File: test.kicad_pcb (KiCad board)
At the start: 2 copper layers, 45.7 x 27.9 mm, 32 parts, among them J1 ICSP, J2 SPI, J3 UART, J4 3.3v VDD, J5 VSS, J6 GPIO Header, J7 I2C, SW1 Reset Button, U1 PIC32MX340F512H-80I_MR

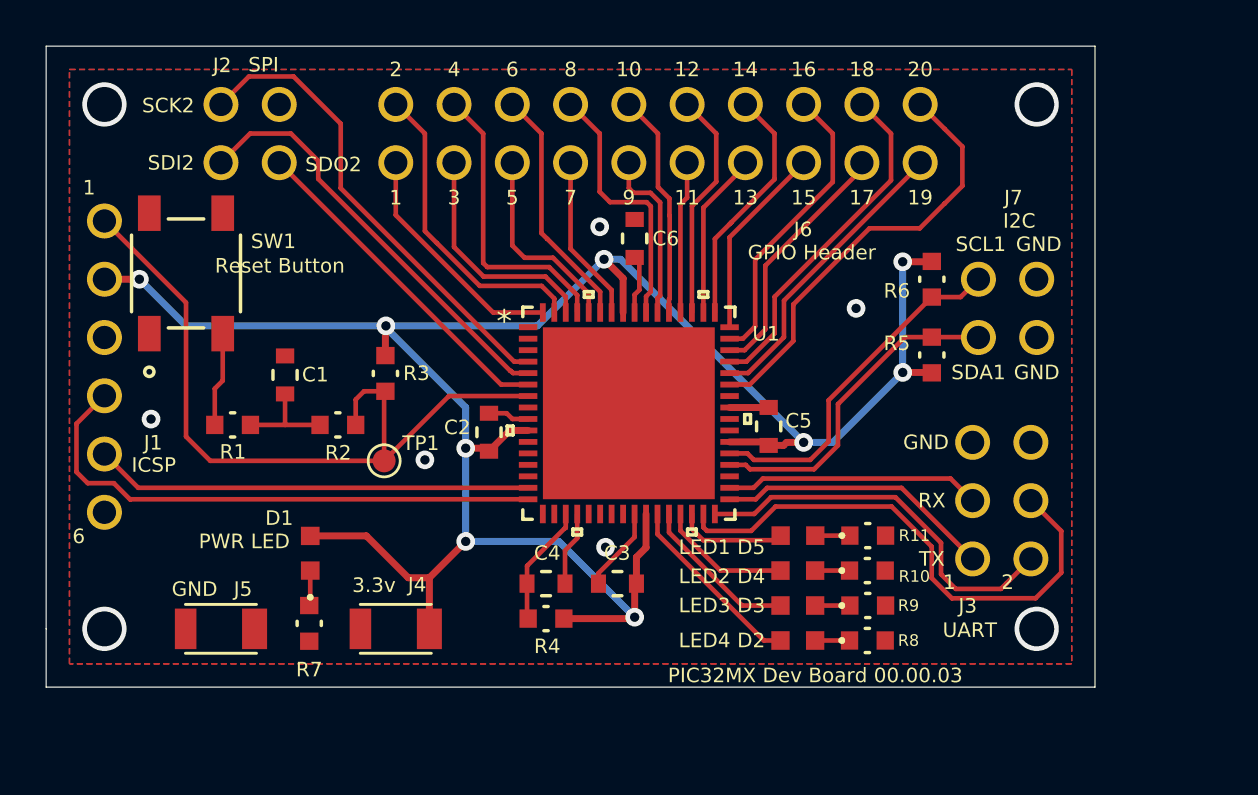
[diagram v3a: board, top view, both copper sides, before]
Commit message: - Changed PIC from MR to PT package for ease of soldering - Increased size from 2"-1.2"
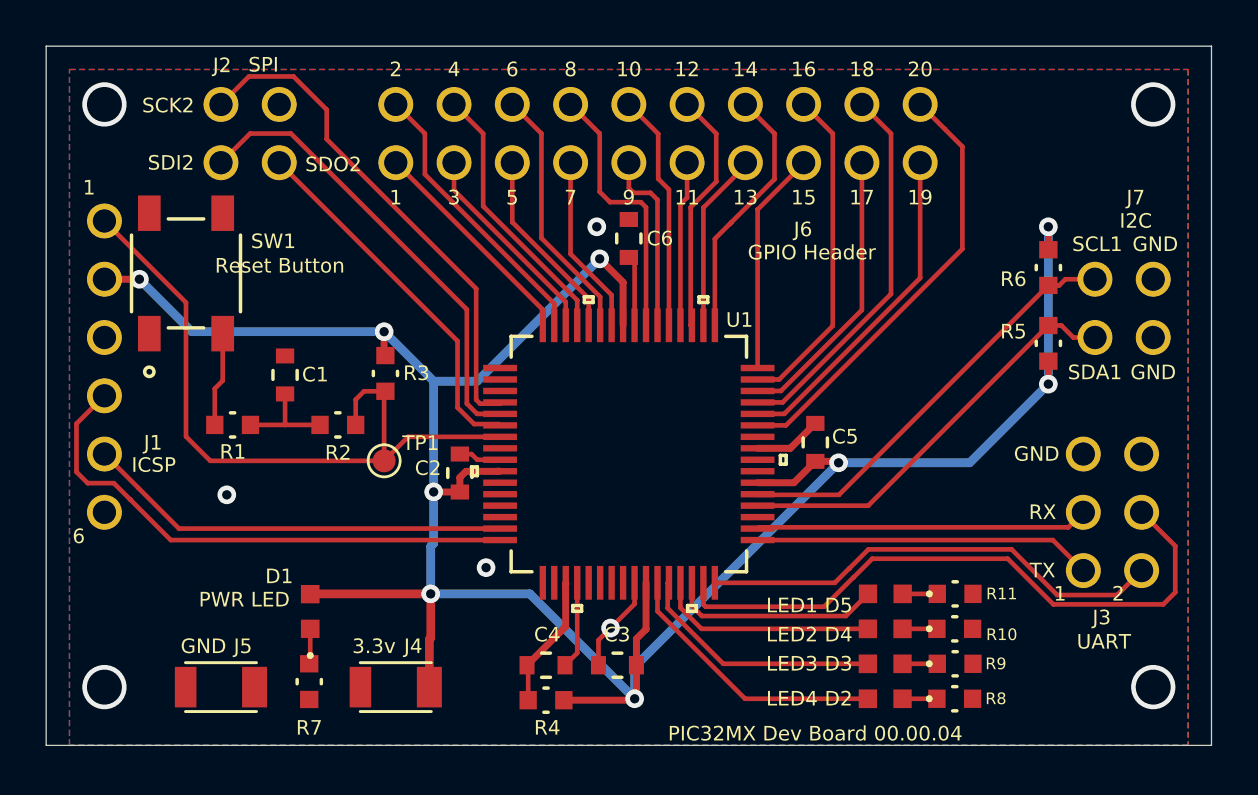
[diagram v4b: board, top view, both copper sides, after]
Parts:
- U1: value PIC32MX340F512H-80I_MR -> PIC32MX340F512H-80V_PT; footprint mod:PIC32MX340F512H-80I&slash_MR -> mod:PIC32MX340F512H-80V&slash_PT
- moved R5 5.11 mm to (180.8, 104.4)
- moved R6 5.11 mm to (180.8, 101.1)
- moved J7 5.08 mm to (182.9, 101.6)
- moved J3 4.85 mm to (182.4, 114.3)
- moved D2 4.58 mm to (173.7, 119.9)
- moved D3 4.58 mm to (173.7, 118.4)
- moved D4 4.58 mm to (173.7, 116.8)
- moved R10 4.58 mm to (176.8, 116.8)
- moved R11 4.58 mm to (176.8, 115.3)
- moved R8 4.58 mm to (176.8, 119.9)
- moved R9 4.58 mm to (176.8, 118.4)
- moved D5 4.58 mm to (173.7, 115.3)
- moved C3 3.56 mm to (162.1, 118.4)
- moved C4 3.56 mm to (158.9, 118.4)
- moved R4 3.56 mm to (158.9, 120.0)
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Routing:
- net +3V3: track 97.3 -> 109.1 mm
- net Net-(D5-Pad2): track 4.81 -> 9.27 mm
- net Net-(J3-Pad3): track 23.3 -> 27.6 mm
- net Net-(D3-Pad2): track 6.98 -> 10.9 mm
- net Net-(D4-Pad2): track 5.81 -> 9.64 mm
- net Net-(D2-Pad2): track 8.16 -> 12.0 mm
- net Net-(J7-Pad1): track 14.4 -> 18.2 mm
- net Net-(J3-Pad1): track 17.1 -> 20.5 mm
- net Net-(J3-Pad4): track 11.2 -> 14.5 mm
- net Net-(J7-Pad2): track 15.3 -> 18.6 mm
- net Net-(J3-Pad2): track 12.1 -> 14.7 mm
- net GNDREF: track 10.5 -> 12.9 mm, vias 9 -> 8
- net Net-(J1-Pad1): track 33.0 -> 31.0 mm
- net Net-(J6-Pad17): track 10.9 -> 12.7 mm
- net Net-(J6-Pad19): track 13.1 -> 14.6 mm
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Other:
- board size 45.7 x 27.9 mm -> 50.8 x 30.5 mm
- board text added: "PIC32MX Dev Board 00.00.04"
- board text removed: "PIC32MX Dev Board 00.00.03"

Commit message: Made a few changes for boardhouse - Moved title silkscreen up like 10mil - Shifted mount holes from vias to an actual footprint
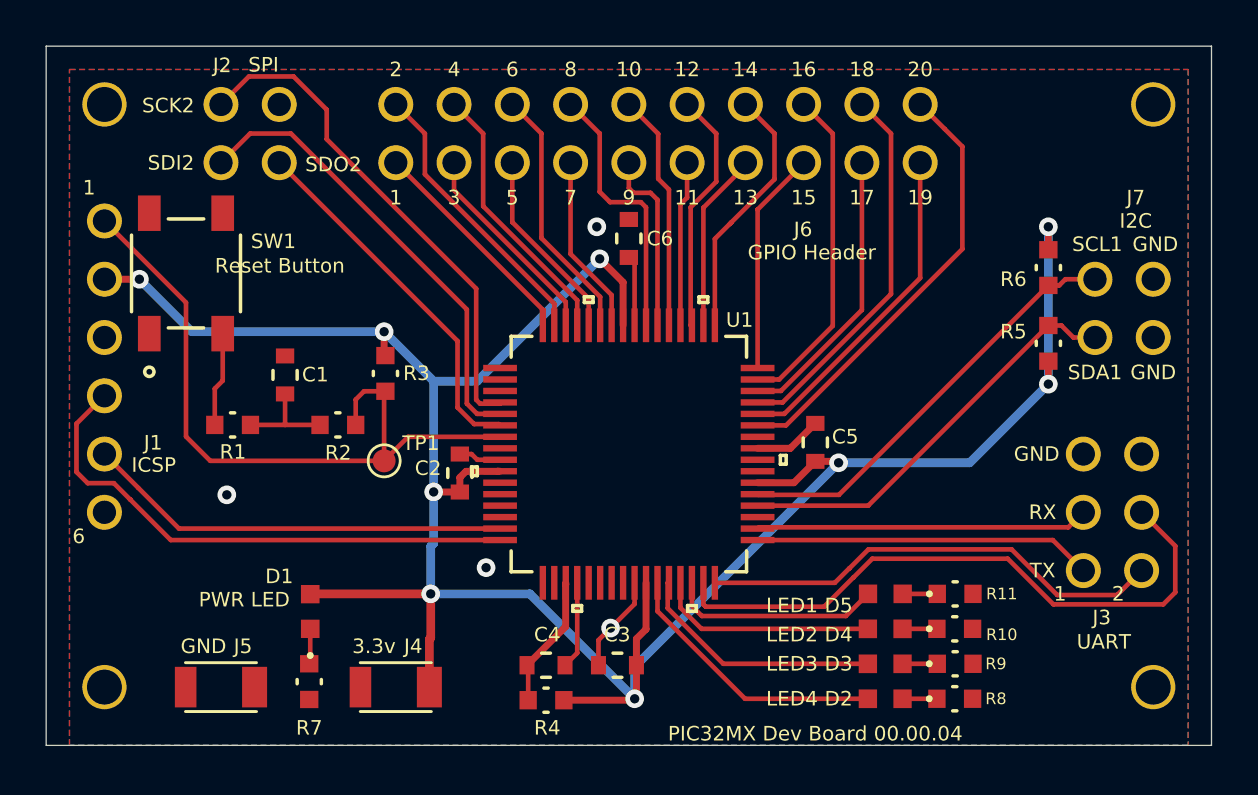
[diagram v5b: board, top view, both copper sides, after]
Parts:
- added H1: MountingHole_Pad, mod:test, F.Cu at (139.7, 94.0)
- added H2: MountingHole_Pad, mod:test, F.Cu at (185.4, 119.4)
- added H3: MountingHole_Pad, mod:test, F.Cu at (185.4, 94.0)
- added H4: MountingHole_Pad, mod:test, F.Cu at (139.7, 119.4)
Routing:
- net GNDREF: vias 8 -> 4
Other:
- rule pad_to_mask_clearance: 0.2 -> 0

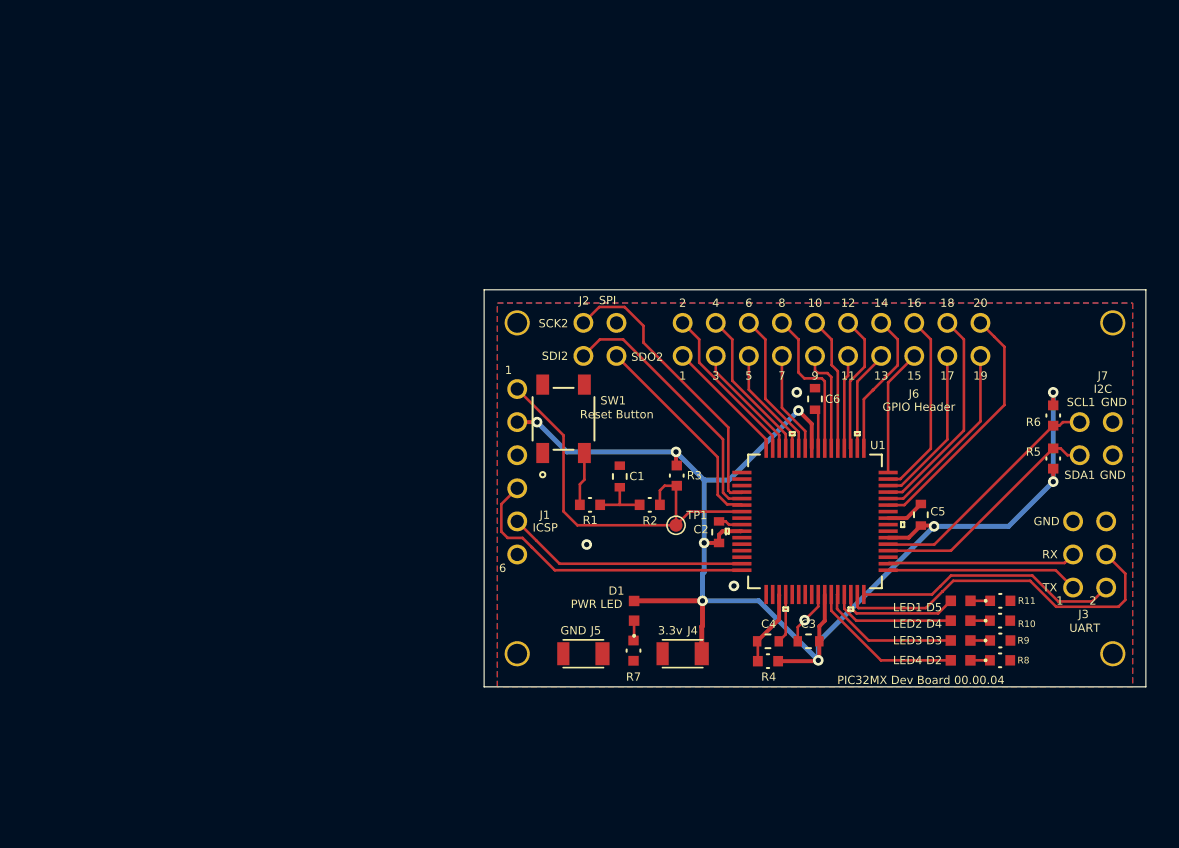
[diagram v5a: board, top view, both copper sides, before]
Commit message: - Began work on dev board V2
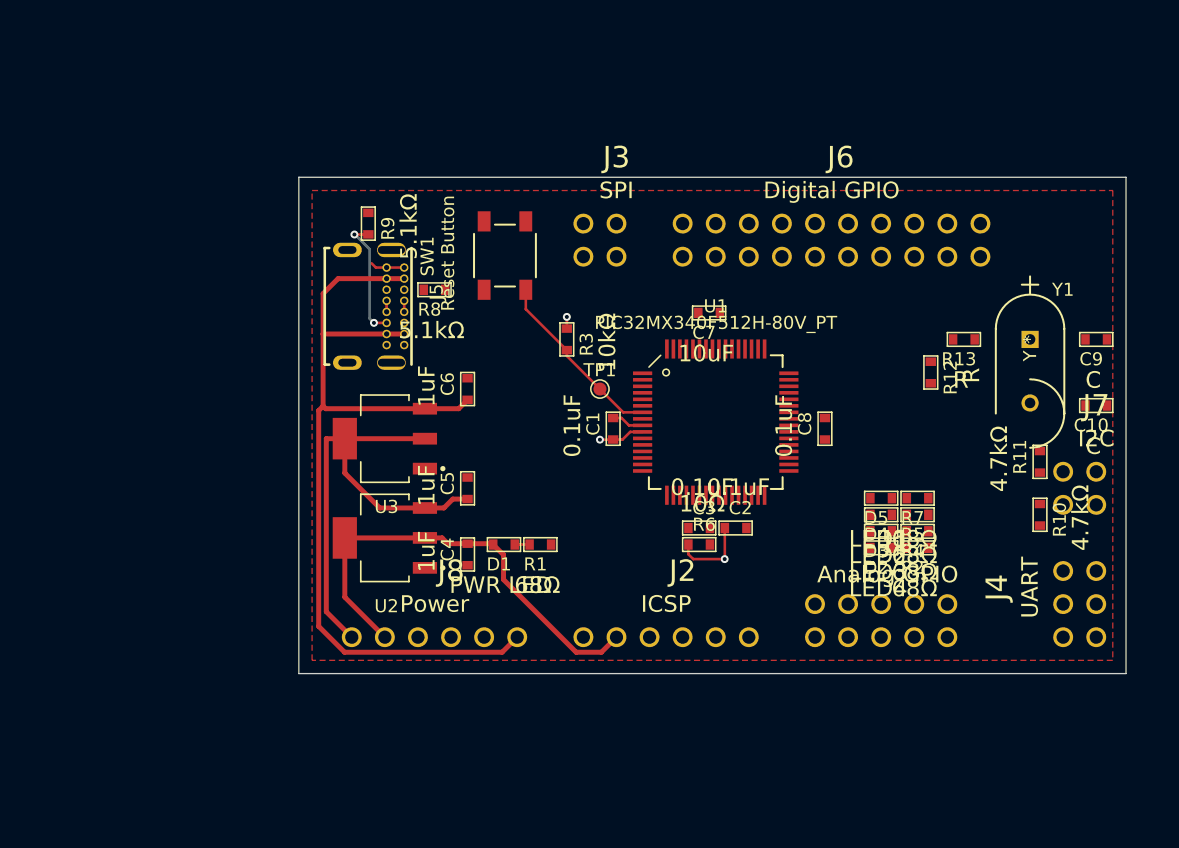
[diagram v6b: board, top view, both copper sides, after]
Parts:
- removed H1, H2, H3, H4: MountingHole_Pad, mod:test
- added C10: C, mod:0603, F.Cu at (184.2, 100.3)
- added C7: 10uF, mod:0603, F.Cu at (154.4, 93.2)
- added C8: 0.1uF, mod:0603, F.Cu at (163.3, 102.1)
- added C9: C, mod:0603, F.Cu at (184.2, 95.2)
- added J8: Power, mod:01x06, F.Cu at (127.0, 118.1)
- added R12: R, mod:0603, F.Cu at (171.4, 97.8)
- added R13: R, mod:0603, F.Cu at (174.0, 95.2)
- added U2: AZ1117EH-3.3TRG1, mod:SOT230P700X180-4N, F.Cu at (129.5, 110.5)
- added U3: AZ1117EH-5.0TRG1, mod:SOT230P700X180-4N, F.Cu at (129.5, 102.9)
- added Y1: Y, mod:9B-8.000MAAJ-B, F.Cu at (179.1, 95.2)
- C1, C2, C3: footprint mod:CL10A106MQ8NNNC -> mod:0603
- C4, C5: value 0.1uF -> 1uF; footprint mod:CL10A106MQ8NNNC -> mod:0603
- C6: value 10uF -> 1uF; footprint mod:CL10A106MQ8NNNC -> mod:0603
- D1, D2, D3, D4, D5: footprint mod:LTST-C191KGKT -> mod:0603
- J1: value ICSP -> Analog GPIO; footprint mod:01x06 -> mod:02x05
- J2: value SPI -> ICSP; footprint mod:02x02 -> mod:01x06
- J3: value UART -> SPI; footprint mod:02x03 -> mod:02x02
- J4: value 3.3v VDD -> UART; footprint mod:RESC3115X65N -> mod:02x03
- J5: value VSS -> USB4085-GF-A_REVA; footprint mod:RESC3115X65N -> mod:GCT_USB4085-GF-A_REVA
- J6: value GPIO Header -> Digital GPIO
- R1, R2: value 470Ω -> 68Ω; footprint mod:ERJ-3EKF10R0V -> mod:0603
- R10, R11: value 68Ω -> 4.7kΩ; footprint mod:ERJ-3EKF10R0V -> mod:0603
- R3, R7: footprint mod:ERJ-3EKF10R0V -> mod:0603
- R4: value 10Ω -> 68Ω; footprint mod:ERJ-3EKF10R0V -> mod:0603
- R5: value 4.7kΩ -> 68Ω; footprint mod:ERJ-3EKF10R0V -> mod:0603
- R6: value 4.7kΩ -> 10Ω; footprint mod:ERJ-3EKF10R0V -> mod:0603
- R8, R9: value 68Ω -> 5.1kΩ; footprint mod:ERJ-3EKF10R0V -> mod:0603
- moved R9 58.1 mm to (128.3, 86.4), turned to 270 degrees
- moved R8 51.9 mm to (133.3, 91.4)
- moved J3 46.8 mm to (144.8, 86.4), turned to 0 degrees
- moved C5 34.9 mm to (135.9, 106.7)
- moved J5 32.1 mm to (127.0, 92.7), turned to 270 degrees
- moved J4 29.2 mm to (181.6, 118.1), turned to 90 degrees
- moved R6 28.9 mm to (153.7, 111.0), turned to 0 degrees
- moved J1 28.2 mm to (162.6, 115.6), turned to 0 degrees
- moved C6 26.7 mm to (135.9, 99.1)
- moved R7 24.7 mm to (170.4, 107.4), turned to 180 degrees
- moved J2 24.1 mm to (144.8, 118.1)
- moved C4 24.0 mm to (135.9, 111.8), turned to 90 degrees
- moved R2 20.8 mm to (170.4, 111.3), turned to 180 degrees
- moved R4 15.2 mm to (170.4, 110.0)
- moved R3 13.4 mm to (143.5, 95.2)
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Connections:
- C1 pad 1: GNDREF -> +3V3
- C1 pad 2: Net-(C1-Pad2) -> GNDREF
- C3 pad 1: +3V3 -> GNDREF
- C3 pad 2: GNDREF -> Net-(C3-Pad2)
- C4 pad 2: Net-(C4-Pad2) -> +3V3
- C5 pad 1: +3V3 -> +5V
- C6 pad 1: Net-(C6-Pad1) -> VCC
- J1 pad 2: +3V3 -> Net-(J1-Pad2)
- J1 pad 3: GNDREF -> Net-(J1-Pad3)
- J2 pad 2: Net-(J2-Pad2) -> +3V3
- J2 pad 3: Net-(J2-Pad3) -> GNDREF
- J4 pad 1: +3V3 -> Net-(J4-Pad1)
- R1 pad 1: Net-(R1-Pad1) -> GNDREF
- R1 pad 2: Net-(C1-Pad2) -> Net-(D1-Pad1)
- R10 pad 1: GNDREF -> Net-(J7-Pad1)
- R10 pad 2: Net-(D4-Pad1) -> +3V3
- R11 pad 1: GNDREF -> Net-(J7-Pad2)
- R11 pad 2: Net-(D5-Pad1) -> +3V3
- R2 pad 1: Net-(C1-Pad2) -> GNDREF
- R2 pad 2: Net-(J1-Pad1) -> Net-(D2-Pad1)
- R3 pad 2: Net-(J1-Pad1) -> Net-(J2-Pad1)
- R4 pad 1: +3V3 -> GNDREF
- R4 pad 2: Net-(C4-Pad2) -> Net-(D3-Pad1)
- R5 pad 1: Net-(J7-Pad1) -> GNDREF
- R5 pad 2: +3V3 -> Net-(D4-Pad1)
- R6 pad 1: Net-(J7-Pad2) -> +3V3
- R6 pad 2: +3V3 -> Net-(C3-Pad2)
- R7 pad 2: Net-(D1-Pad1) -> Net-(D5-Pad1)
- R8 pad 2: Net-(D2-Pad1) -> Net-(J5-PadA5)
- R9 pad 2: Net-(D3-Pad1) -> Net-(J5-PadB5)
- SW1 pad 3: Net-(R1-Pad1) -> Net-(J2-Pad1)
- TP1 pad 1: Net-(J1-Pad1) -> Net-(J2-Pad1)
- U1 pad 11: Net-(U1-Pad11) -> Net-(J1-Pad6)
- U1 pad 12: Net-(U1-Pad12) -> Net-(J1-Pad5)
- U1 pad 13: Net-(U1-Pad13) -> Net-(J1-Pad4)
- U1 pad 14: Net-(U1-Pad14) -> Net-(J1-Pad3)
- U1 pad 15: Net-(J1-Pad5) -> Net-(J1-Pad2)
- U1 pad 16: Net-(J1-Pad4) -> Net-(J1-Pad1)
- U1 pad 17: Net-(U1-Pad17) -> Net-(J2-Pad5)
- U1 pad 18: Net-(U1-Pad18) -> Net-(J2-Pad4)
- U1 pad 19: Net-(C4-Pad2) -> Net-(C3-Pad2)
- U1 pad 21: Net-(U1-Pad21) -> Net-(J1-Pad7)
- U1 pad 22: Net-(U1-Pad22) -> Net-(J1-Pad8)
- U1 pad 23: Net-(U1-Pad23) -> Net-(J1-Pad9)
- U1 pad 24: Net-(U1-Pad24) -> Net-(J1-Pad10)
- U1 pad 31: Net-(J3-Pad3) -> Net-(J4-Pad3)
- U1 pad 32: Net-(J3-Pad1) -> Net-(J4-Pad1)
- U1 pad 33: Net-(J3-Pad2) -> Net-(J4-Pad2)
- U1 pad 34: Net-(J3-Pad4) -> Net-(J4-Pad4)
- U1 pad 4: Net-(J2-Pad2) -> Net-(J3-Pad2)
- U1 pad 5: Net-(J2-Pad1) -> Net-(J3-Pad1)
- U1 pad 56: Net-(C6-Pad1) -> Net-(C7-Pad1)
- U1 pad 6: Net-(J2-Pad3) -> Net-(J3-Pad3)
- U1 pad 7: Net-(J1-Pad1) -> Net-(J2-Pad1)
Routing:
- net VCC: track 0.00 -> 66.6 mm
- net +3V3: track 109.1 -> 45.5 mm, vias 9 -> 3
- net +5V: track 0.00 -> 37.1 mm
- net Net-(J1-Pad1): track 31.0 -> 0.00 mm
- net Net-(J3-Pad3): track 27.6 -> 0.00 mm
- net Net-(J1-Pad4): track 23.5 -> 0.00 mm
- net Net-(J2-Pad2): track 22.2 -> 0.00 mm
- net Net-(J3-Pad1): track 20.5 -> 0.00 mm
- net Net-(J6-Pad20): track 19.2 -> 0.00 mm
- net Net-(J7-Pad2): track 18.6 -> 0.00 mm
- net Net-(J1-Pad5): track 18.6 -> 0.00 mm
- net Net-(J7-Pad1): track 18.2 -> 0.00 mm
- net Net-(J2-Pad3): track 16.6 -> 0.00 mm
- net Net-(J6-Pad18): track 16.6 -> 0.00 mm
- net Net-(J3-Pad2): track 14.7 -> 0.00 mm
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- removed copper zone on B.Cu, net GNDREF
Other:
- board size 50.8 x 30.5 mm -> 63.5 x 38.1 mm
- net class Default: via_dia 0.8128 -> 0.6096; via_drill 0.4064 -> 0.3048
- rule via_min_drill: 0.3 -> 0.3048
- rule via_min_size: 0.4064 -> 0.6096
- board text removed: "1"
- board text removed: "10"
- board text removed: "11"
- board text removed: "12"
- board text removed: "13"
- board text removed: "14"
- board text removed: "15"
- board text removed: "16"
- board text removed: "17"
- board text removed: "18"
- board text removed: "19"
- board text removed: "2"
- board text removed: "20"
- board text removed: "3"
- board text removed: "3.3v"
- board text removed: "4"
- board text removed: "5"
- board text removed: "6"
- board text removed: "7"
- board text removed: "8"
- board text removed: "9"
- board text removed: "GND"
- board text removed: "PIC32MX Dev Board 00.00.04"
- board text removed: "RX"
- board text removed: "SCK2"
- board text removed: "SCL1"
- board text removed: "SDA1"
- board text removed: "SDI2"
- board text removed: "SDO2"
- board text removed: "TX"
